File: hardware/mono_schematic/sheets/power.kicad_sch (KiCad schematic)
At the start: 33 parts

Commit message: mono_electronics v11b: TLV75733P 1A AON LDO, 22uF ESP32 bulk, LED_EN RC glitch filter, J_USB value, refs end in digit; schematic regenerated (ERC 0, 0 diffs)
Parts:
- removed C_ASW_IN, C_AUD_SW, C_LL_IN: 1u, mono_electronics:C_0402_1005Metric, symbol mono_parts:1u_C_0402_1005Metric_2
- removed C_CHG_BAT, C_CHG_IN, C_CHG_SYS, C_SYS: 10u, mono_electronics:C_0805_2012Metric, symbol mono_parts:10u_C_0805_2012Metric_2
- removed C_GAUGE: 100n, mono_electronics:C_0402_1005Metric, symbol mono_parts:100n_C_0402_1005Metric_2
- removed C_LDO_IN, C_LDO_OUT: 1u, mono_electronics:C_0603_1608Metric, symbol mono_parts:1u_C_0603_1608Metric_2
- removed J_BAT: 53398-0371, mono_electronics:Molex_PicoBlade_53398-0371_1x03-1MP_P1.25mm_Vertical, symbol mono_parts:53398-0371_Molex_PicoBlade_53398-0371_1x03-1MP_P1.25mm_Vertical_3
- removed L_LED: DFE201612E-R47M, mono_electronics:L_Murata_DFE201610P, symbol mono_parts:DFE201612E-R47M_L_Murata_DFE201610P_2
- removed R_ALRT: 10k, mono_electronics:R_0402_1005Metric, symbol mono_parts:10k_R_0402_1005Metric_2
- removed R_AUD_PD, R_EN_PD, R_LOGIC_PD: 100k, mono_electronics:R_0402_1005Metric, symbol mono_parts:100k_R_0402_1005Metric_2
- removed R_FB_BOT: 91k, mono_electronics:R_0402_1005Metric, symbol mono_parts:91k_R_0402_1005Metric_2
- removed R_FB_TOP: 681k, mono_electronics:R_0402_1005Metric, symbol mono_parts:681k_R_0402_1005Metric_2
- removed R_ILIM: 18k, mono_electronics:R_0402_1005Metric, symbol mono_parts:18k_R_0402_1005Metric_2
- removed R_ISET: 600R, mono_electronics:R_0402_1005Metric, symbol mono_parts:600R_R_0402_1005Metric_2
- removed R_QOD: 1k, mono_electronics:R_0402_1005Metric, symbol mono_parts:1k_R_0402_1005Metric_2
- removed R_TH: 10k 1%, mono_electronics:R_0402_1005Metric, symbol mono_parts:10k_1__R_0402_1005Metric_2
- removed TH_PCB: NTC 10k B3435, mono_electronics:R_0402_1005Metric, symbol mono_parts:NTC_10k_B3435_R_0402_1005Metric_2
- removed U_AUDIO_SW: TPS22917, mono_electronics:SOT-23-6, symbol mono_parts:TPS22917_SOT-23-6_4
- removed U_CHG: BQ25185, mono_electronics:Texas_DLH0010A_WSON-10-1EP_2x2mm_P0.4mm_EP0.9x1.5mm, symbol mono_parts:BQ25185_Texas_DLH0010A_WSON-10-1EP_2x2mm_P0.4mm_EP0.9x1.5mm_9
- removed U_GAUGE: MAX17048G+T10, mono_electronics:TDFN-8-1EP_2x2mm_P0.5mm_EP0.8x1.2mm, symbol mono_parts:MAX17048G_T10_TDFN-8-1EP_2x2mm_P0.5mm_EP0.8x1.2mm_9
- removed U_LDO: TPS7A2033, mono_electronics:SOT-23-5, symbol mono_parts:TPS7A2033_SOT-23-5_4
- removed U_LED_LOGIC: TPS22917, mono_electronics:SOT-23-6, symbol mono_parts:TPS22917_SOT-23-6_5
- removed U_LED_PWR: TPS63802DLAR, mono_electronics:TDFN-10-1EP_2x3mm_P0.5mm_EP0.9x2mm, symbol mono_parts:TPS63802DLAR_TDFN-10-1EP_2x3mm_P0.5mm_EP0.9x2mm_10
- added C_ASW_IN1, C_AUD_SW1, C_LL_IN1: 1u, mono_electronics:C_0402_1005Metric, symbol mono_parts:1u_C_0402_1005Metric_2
- added C_CHG_BAT1, C_CHG_IN1, C_CHG_SYS1, C_SYS1: 10u, mono_electronics:C_0805_2012Metric, symbol mono_parts:10u_C_0805_2012Metric_2
- added C_EN1: 10n, mono_electronics:C_0402_1005Metric, symbol mono_parts:10n_C_0402_1005Metric_2
- added C_GAUGE1: 100n, mono_electronics:C_0402_1005Metric, symbol mono_parts:100n_C_0402_1005Metric_2
- added C_LDO_IN1, C_LDO_OUT1: 1u, mono_electronics:C_0603_1608Metric, symbol mono_parts:1u_C_0603_1608Metric_2
- added J_BAT1: 53398-0371, mono_electronics:Molex_PicoBlade_53398-0371_1x03-1MP_P1.25mm_Vertical, symbol mono_parts:53398-0371_Molex_PicoBlade_53398-0371_1x03-1MP_P1.25mm_Vertical_3
- added L_LED1: DFE201612E-R47M, mono_electronics:L_Murata_DFE201610P, symbol mono_parts:DFE201612E-R47M_L_Murata_DFE201610P_2
- added R_ALRT1: 10k, mono_electronics:R_0402_1005Metric, symbol mono_parts:10k_R_0402_1005Metric_2
- added R_AUD_PD1, R_LOGIC_PD1: 100k, mono_electronics:R_0402_1005Metric, symbol mono_parts:100k_R_0402_1005Metric_2
- added R_FB_BOT1: 91k, mono_electronics:R_0402_1005Metric, symbol mono_parts:91k_R_0402_1005Metric_2
- added R_FB_TOP1: 681k, mono_electronics:R_0402_1005Metric, symbol mono_parts:681k_R_0402_1005Metric_2
- added R_ILIM1: 18k, mono_electronics:R_0402_1005Metric, symbol mono_parts:18k_R_0402_1005Metric_2
- added R_ISET1: 600R, mono_electronics:R_0402_1005Metric, symbol mono_parts:600R_R_0402_1005Metric_2
- added R_QOD1: 1k, mono_electronics:R_0402_1005Metric, symbol mono_parts:1k_R_0402_1005Metric_2
- added R_TH1: 10k 1%, mono_electronics:R_0402_1005Metric, symbol mono_parts:10k_1__R_0402_1005Metric_2
- added TH_PCB1: NTC 10k B3435, mono_electronics:R_0402_1005Metric, symbol mono_parts:NTC_10k_B3435_R_0402_1005Metric_2
- added U_AUDIO_SW1: TPS22917, mono_electronics:SOT-23-6, symbol mono_parts:TPS22917_SOT-23-6_4
- added U_CHG1: BQ25185, mono_electronics:Texas_DLH0010A_WSON-10-1EP_2x2mm_P0.4mm_EP0.9x1.5mm, symbol mono_parts:BQ25185_Texas_DLH0010A_WSON-10-1EP_2x2mm_P0.4mm_EP0.9x1.5mm_9
- added U_GAUGE1: MAX17048G+T10, mono_electronics:TDFN-8-1EP_2x2mm_P0.5mm_EP0.8x1.2mm, symbol mono_parts:MAX17048G_T10_TDFN-8-1EP_2x2mm_P0.5mm_EP0.8x1.2mm_9
- added U_LDO1: TLV75733PDBVR, mono_electronics:SOT-23-5, symbol mono_parts:TLV75733PDBVR_SOT-23-5_4
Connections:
- net AON_3V3: now also C_ASW_IN1.1, C_LDO_OUT1.1, C_LL_IN1.1, R_ALRT1.2, R_TH1.2, U_AUDIO_SW1.1 (AON_3V3), U_LDO1.5 (AON_3V3)
- net AUDIO_3V3: now also C_AUD_SW1.1, U_AUDIO_SW1.6 (AUDIO_3V3)
- net AUDIO_EN: now also R_AUD_PD1.1, U_AUDIO_SW1.3 (AUDIO_EN)
- net BAT_RAW: now also C_CHG_BAT1.2, C_GAUGE1.2, J_BAT1.1 (BAT_RAW), U_CHG1.2 (BAT_RAW), U_GAUGE1.2 (BAT_RAW), U_GAUGE1.3 (BAT_RAW)
- net GAUGE_ALRT_N: now also R_ALRT1.1, U_GAUGE1.5 (GAUGE_ALRT_N)
- net GND: now also C_ASW_IN1.2, C_AUD_SW1.2, C_CHG_BAT1.1, C_CHG_IN1.2, C_CHG_SYS1.1, C_EN1.2, C_GAUGE1.1, C_LDO_IN1.1, C_LDO_OUT1.2, C_LL_IN1.2, C_SYS1.2, J_BAT1.3 (GND), R_AUD_PD1.2, R_FB_BOT1.2, R_ILIM1.2, R_ISET1.2, R_LOGIC_PD1.2, TH_PCB1.1, U_AUDIO_SW1.2 (GND), U_CHG1.11 (GND), U_CHG1.4 (GND), U_CHG1.5 (GND), U_GAUGE1.1 (GND), U_GAUGE1.4 (GND), U_GAUGE1.6 (GND), U_GAUGE1.9 (GND), U_LDO1.2 (GND)
- net ILIM_VSET: now also R_ILIM1.1, U_CHG1.7 (ILIM_VSET)
- net IMU_SCL: now also U_GAUGE1.7 (IMU_SCL)
- net IMU_SDA: now also U_GAUGE1.8 (IMU_SDA)
- net ISET: now also R_ISET1.1, U_CHG1.8 (ISET)
- net LED_4V1: now also R_FB_TOP1.1
- net LED_FB: now also R_FB_BOT1.1, R_FB_TOP1.2
- net LED_LOGIC_3V3: now also R_QOD1.2
- net LED_LOGIC_EN: now also R_LOGIC_PD1.1
- net LED_QOD: now also R_QOD1.1
- net SW_L1: now also L_LED1.2
- net SW_L2: now also L_LED1.1
- net SYS: now also C_CHG_SYS1.2, C_LDO_IN1.2, C_SYS1.1, U_CHG1.1 (SYS), U_LDO1.1 (SYS), U_LDO1.3 (SYS)
- net TH_ADC: now also R_TH1.1, TH_PCB1.2
- net TS_MR: now also J_BAT1.2 (TS_MR), U_CHG1.6 (TS_MR)
- net VBUS: now also C_CHG_IN1.1, U_CHG1.10 (VBUS)
- new net LED_EN_RC: C_EN1.1

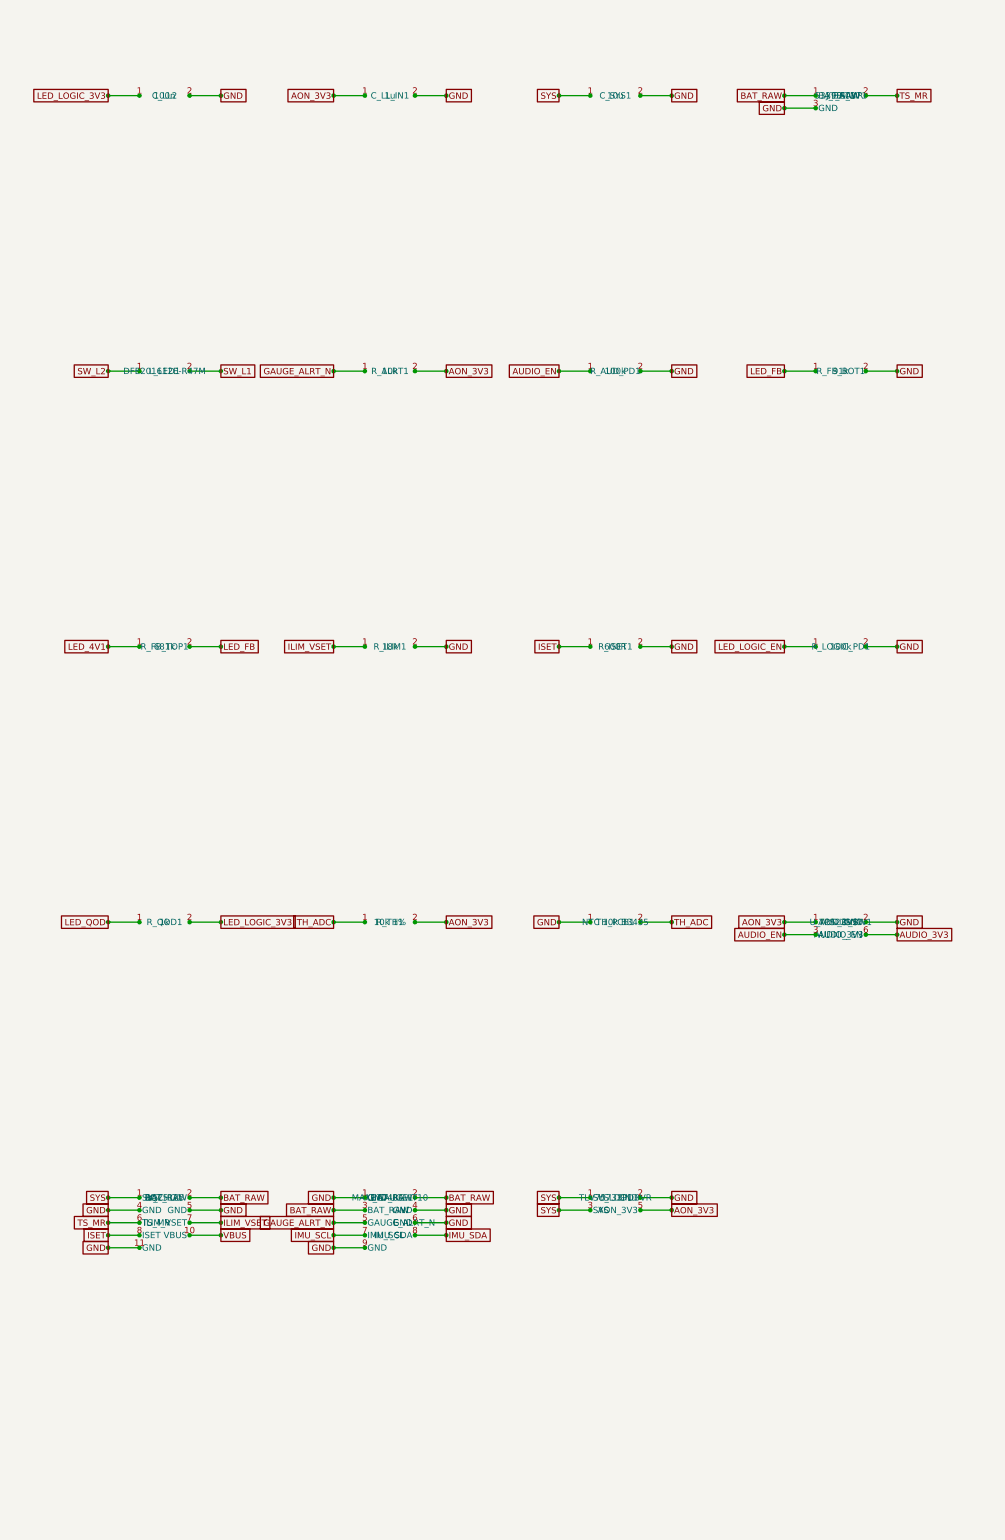
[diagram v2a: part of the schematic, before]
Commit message: mono_electronics v13 chunk1: battery protection — F_BAT1 0466002.NRHF 2A fast fuse at J_BAT1, Q_BAT1 AO3401A ideal-diode reverse-battery P-FET (+R_BATG1 10k), BAT path 1.0 mm on F, In1 BAT_RAW 0.8 mm; GND stitch vias moved; schematic regen (ERC 0, 0 diffs); DRC 0/0/0
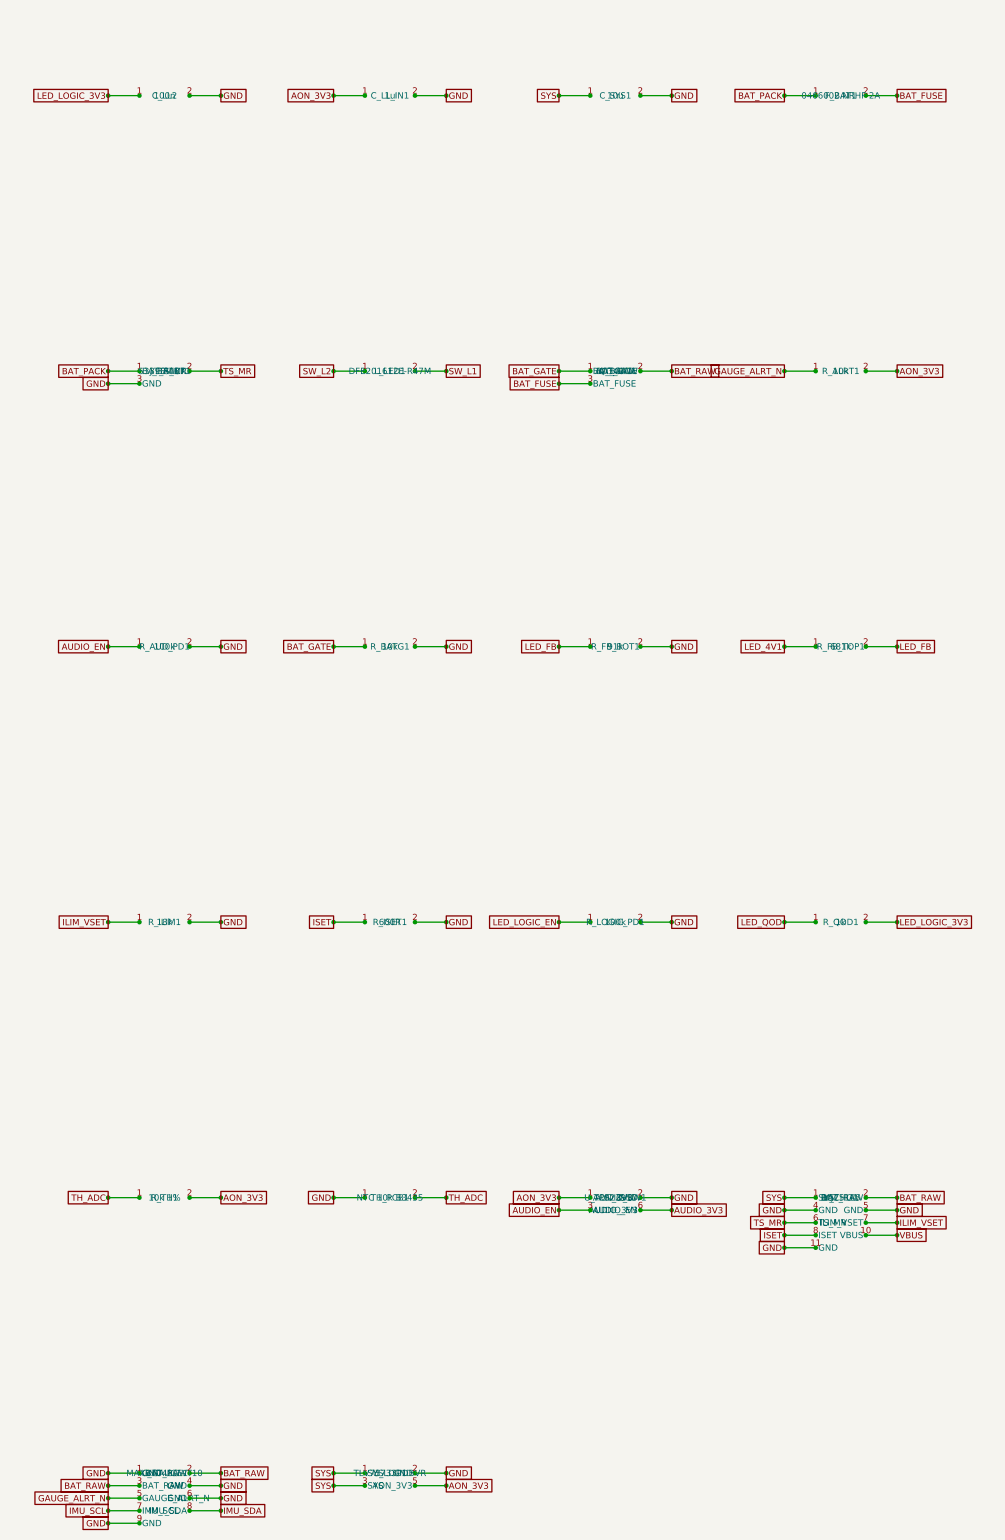
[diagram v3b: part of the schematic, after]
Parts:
- added F_BAT1: 0466002.NRHF 2A, mono_electronics:Fuse_1206_3216Metric, symbol mono_parts:0466002.NRHF_2A_Fuse_1206_3216Metric_2
- added Q_BAT1: AO3401A, mono_electronics:SOT-23, symbol mono_parts:AO3401A_SOT-23_3
- added R_BATG1: 10k, mono_electronics:R_0402_1005Metric, symbol mono_parts:10k_R_0402_1005Metric_2
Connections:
- net BAT_RAW: now also Q_BAT1.2 (BAT_RAW); no longer J_BAT1.1 (BAT_RAW)
- net GND: now also R_BATG1.2
- new net BAT_FUSE: F_BAT1.2, Q_BAT1.3 (BAT_FUSE)
- new net BAT_GATE: Q_BAT1.1 (BAT_GATE), R_BATG1.1
- new net BAT_PACK: F_BAT1.1, J_BAT1.1 (BAT_PACK)

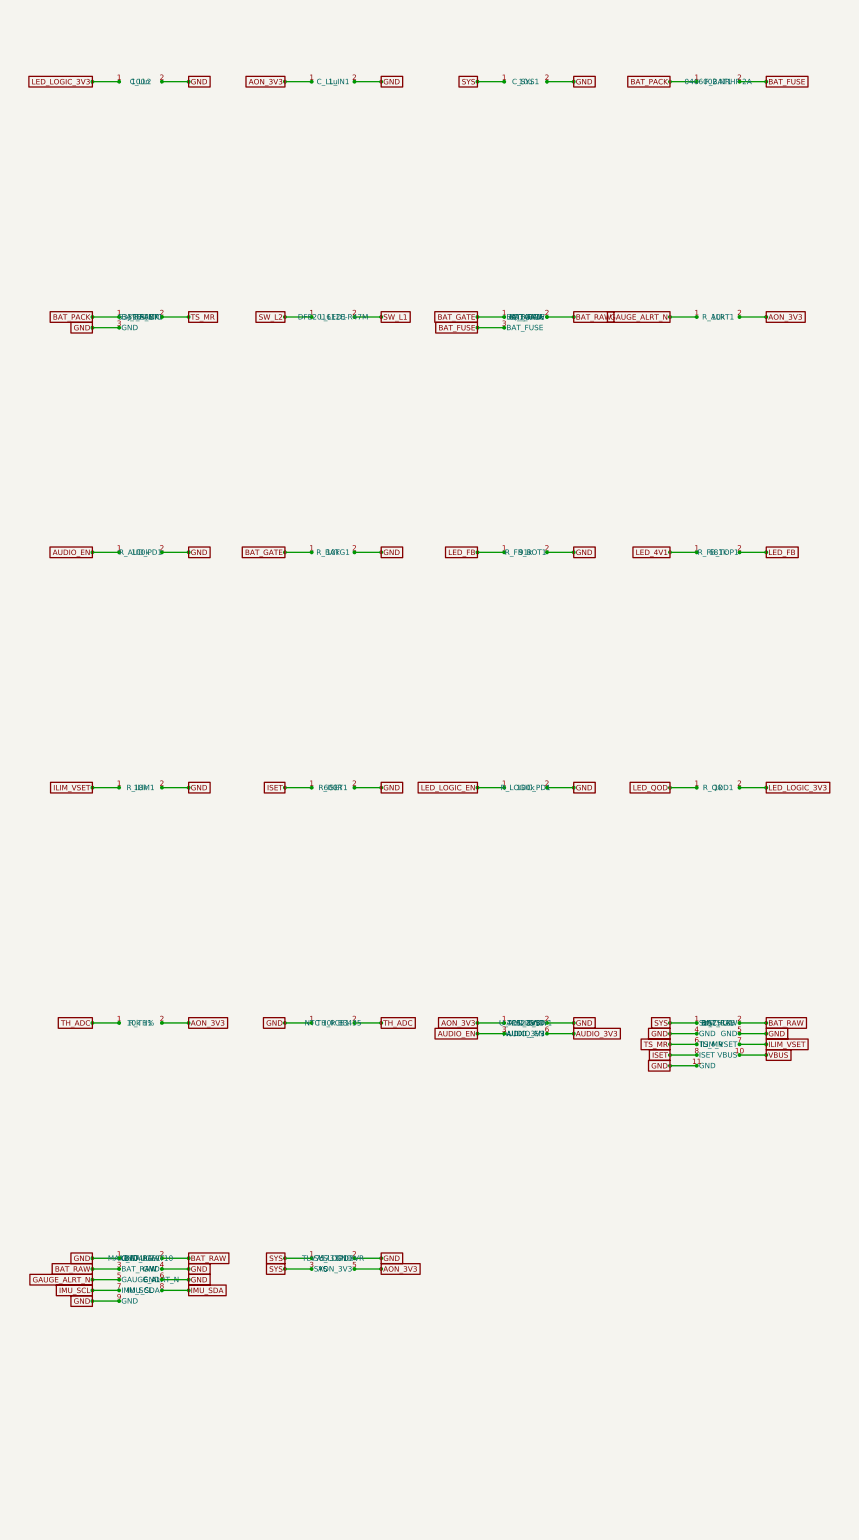
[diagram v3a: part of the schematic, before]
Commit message: mono_electronics v13 chunk2: USB input OVP — U_OVP1 TPS259531DSGR eFuse (5.7 V OV clamp, 1.17 A limit R_ILM1 1.78k, UVLO 4.28 V via 100k/39k), D_VBUS1 SMF12A TVS on VBUS_CONN; USBLC6 now on protected VBUS; schematic regen (ERC 0, 0 diffs); DRC 0/0/0
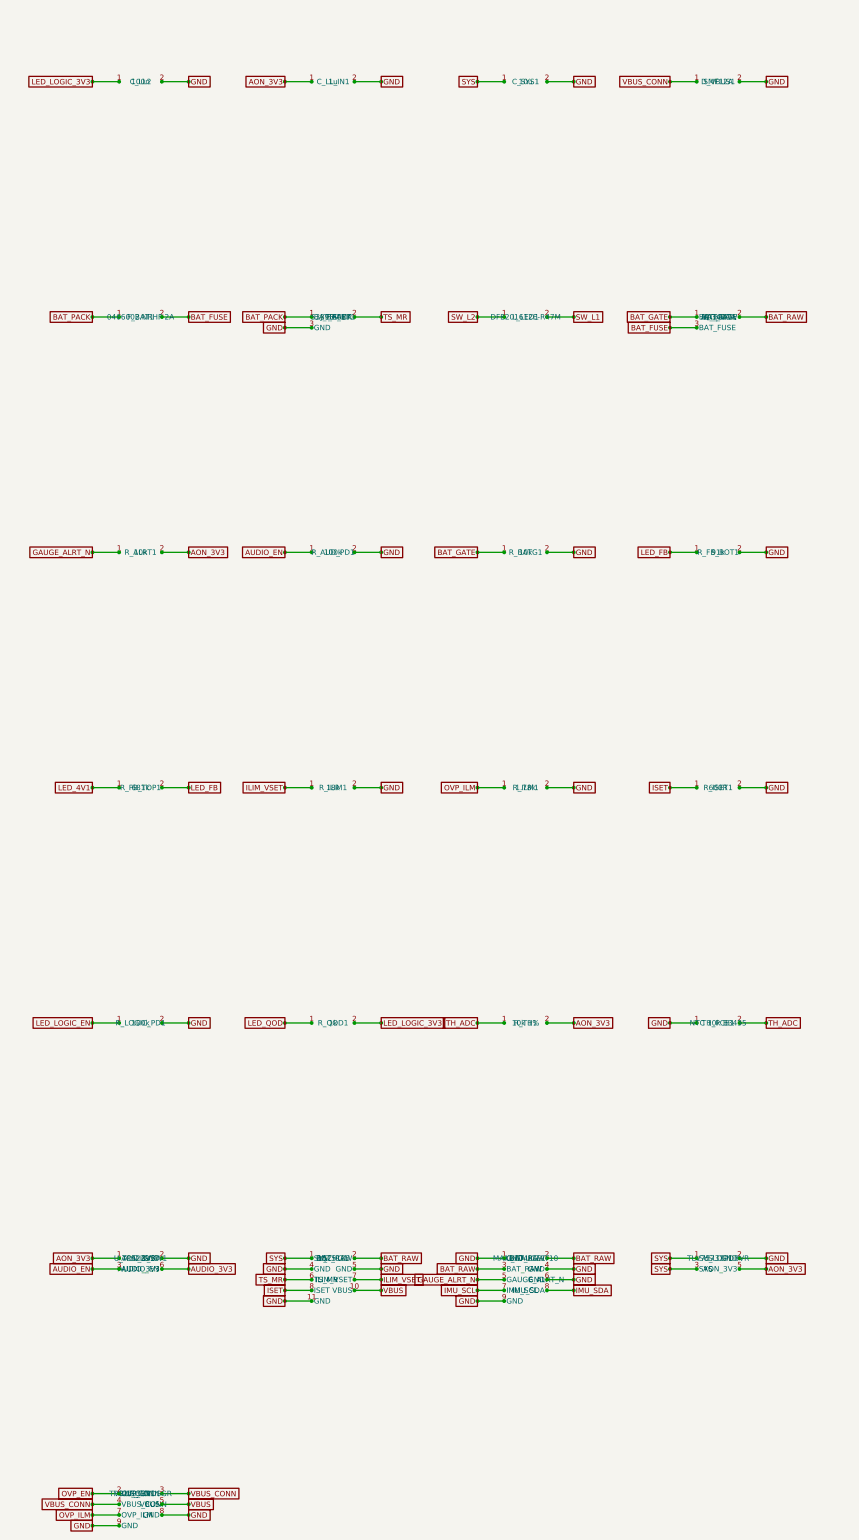
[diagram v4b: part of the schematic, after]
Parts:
- added D_VBUS1: SMF12A, mono_electronics:D_SOD-123F, symbol mono_parts:SMF12A_D_SOD-123F_2
- added R_ILM1: 1.78k, mono_electronics:R_0402_1005Metric, symbol mono_parts:1.78k_R_0402_1005Metric_2
- added U_OVP1: TPS259531DSGR, mono_electronics:Texas_DSG0008A_WSON-8-1EP_2x2mm_P0.5mm_EP0.9x1.6mm, symbol mono_parts:TPS259531DSGR_Texas_DSG0008A_WSON-8-1EP_2x2mm_P0.5mm_EP0.9x1.6mm_7
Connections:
- net GND: now also D_VBUS1.2, R_ILM1.2, U_OVP1.8 (GND), U_OVP1.9 (GND)
- net VBUS: now also U_OVP1.5 (VBUS)
- new net OVP_EN: U_OVP1.2 (OVP_EN)
- new net OVP_ILM: R_ILM1.1, U_OVP1.7 (OVP_ILM)
- new net VBUS_CONN: D_VBUS1.1, U_OVP1.3 (VBUS_CONN), U_OVP1.4 (VBUS_CONN)
